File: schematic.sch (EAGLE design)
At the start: 54 parts, among them J1 FTDI_DEVICERA_SMT, M1 WIRELESS-NRF24L01, Q1 8MHz, T1 NMOS, T2 NMOS, T3 NMOS, T4 NMOS, U1 ATMEGA328P_TQFP, U2 GY-521MPU6050, U3 TPS63060

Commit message: Fixed issues mentioned in design review
Changed voltage divider resistors to 10K.
Got new voltage regulator, completely circuit and PCD footprint.
Changed all component package to 0603.
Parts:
- removed C16: 10uF, resistor:C-USC0805K
- removed C17: 0.1uF, resistor:C-USC0201
- added C15: 0.1uF, resistor:C-USC0603
- added R14: 10K, resistor:R-US_R0603
- added R15, R16: 10K, resistor:R-US_M2309
- C12: value 0.1uF -> 27pF; device rcl:C-USC0603 -> resistor:C-USC0603
- C14: value 27pF -> 10uF
- C2: value 10uF -> 0.056uF; device resistor:C-USC0805K -> resistor:C-USC0603
- C3: device resistor:C-USC0805K -> resistor:C-USC0603
- C4: value 0.1uF -> 100pF; device rcl:C-USC0603 -> resistor:C-USC0603
- C5: value 10pF -> 22uF; device rcl:C-USC0603 -> resistor:C-USC0603
- C6: value 22uF -> 470pF; device rcl:C-USC0603 -> resistor:C-USC0603
- C7: value 22uF -> 10pF; device rcl:C-USC0603 -> resistor:C-USC0603
- C8: value 22uF -> 0.1uF
- L1: value 1uH -> 3.3uH
- R11: value 10K -> 820; device resistor:R-US_R0603 -> rcl:R-US_R0603
- R12: value 10K -> 820; device resistor:R-US_M2309 -> rcl:R-US_R0603
- R13: device resistor:R-US_M2309 -> resistor:R-US_R0603
- R2: value 50K -> 10K; device resistor:R-US_M2309 -> resistor:R-US_R0603
- R3: value 150K -> 10K; device resistor:R-US_R0805 -> resistor:R-US_R0603
- R4: value 560K -> 200K; device rcl:R-US_R0805 -> resistor:R-US_R0603
- R5: value 100K -> 10K; device rcl:R-US_R0402 -> resistor:R-US_R0603
- R6: value 820 -> 374K; device rcl:R-US_R0603 -> resistor:R-US_R0603
- R7: value 10K -> 15K
- R8: value 820 -> 162K; device rcl:R-US_R0603 -> resistor:R-US_R0603
- S2: value (none) -> PUSH_BUTTON
- U3: value TPS63060 -> LTC3534; device SparkFun-PowerIC:TPS63060 -> LTC3534:LTC3534
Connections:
- removed net N$27: L1.1, U3.L1
- removed net N$28: L1.2, U3.L2
- removed net N$32: C5.1, R4.1, R5.2, U3.FB
- removed net N$33: C4.1, U3.VAUX
- new net N$15: C4.1, R5.1
- new net N$16: C2.1, R4.1, U3.RUN/SS
- new net N$18: C4.2, C7.2, R6.1, R7.1, R8.2, U3.FB
- new net N$19: C6.1, C7.1, U3.VC
- new net N$20: C6.2, R7.2
- new net N$8: L1.1, U3.SW1
- new net N$9: L1.2, U3.SW2
- net DEBUG_LED1: now also R12.2; no longer R9.2
- net DEBUG_LED2: now also R11.2; no longer R8.2
- net DTR: now also C8.1; no longer C9.1
- net GND: now also C15.2, C9.2, R13.1, R14.1, R15.2, R16.2, R8.1, U3.GND1, U3.GND2, U3.GND3, U3.GND4, U3.GND5, U3.PGND1, U3.PGND2; no longer C16.2, C17.2, C4.2, C6.2, C7.2, C8.2, R10.1, R11.1, R12.2, R13.2, R5.1, U3.GND, U3.PGND@1, U3.PGND@2, U3.PGND@3, U3.PGND@4, U3.PGND@5, U3.PGND@6, U3.PGND@7, U3.PGND@8, U3.PGND@PAD, U3.PS/SYNC
- net N$1: now also C12.1; no longer C13.1
- net N$11: now also R9.1; no longer R6.1
- net N$12: now also R12.1; no longer R9.1
- net N$13: now also R11.1; no longer R8.1
- net N$2: now also C8.2, R10.1; no longer C9.2, R7.1
- net N$25: now also C11.1; no longer C12.1
- net N$4: now also C13.1; no longer C14.1
- net PWM1: now also R13.2; no longer R10.2
- net PWM2: now also R14.2; no longer R11.2
- net PWM3: now also R15.1; no longer R12.1
- net PWM4: now also R16.1; no longer R13.1
- net PWR: now also R4.2, U3.PVIN, U3.PWM; no longer C2.1, U3.EN
- net V_REG_OUT: now also C14.1, C15.1, C5.1, C9.1, R10.2, R5.2, R9.2; no longer C11.1, C16.1, C17.1, C6.1, C7.1, C8.1, R4.2, R7.2
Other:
- moved on the sheet: C1, C10, C11, C12, C13, C14, C2, C3, C4, C5, C6, C7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

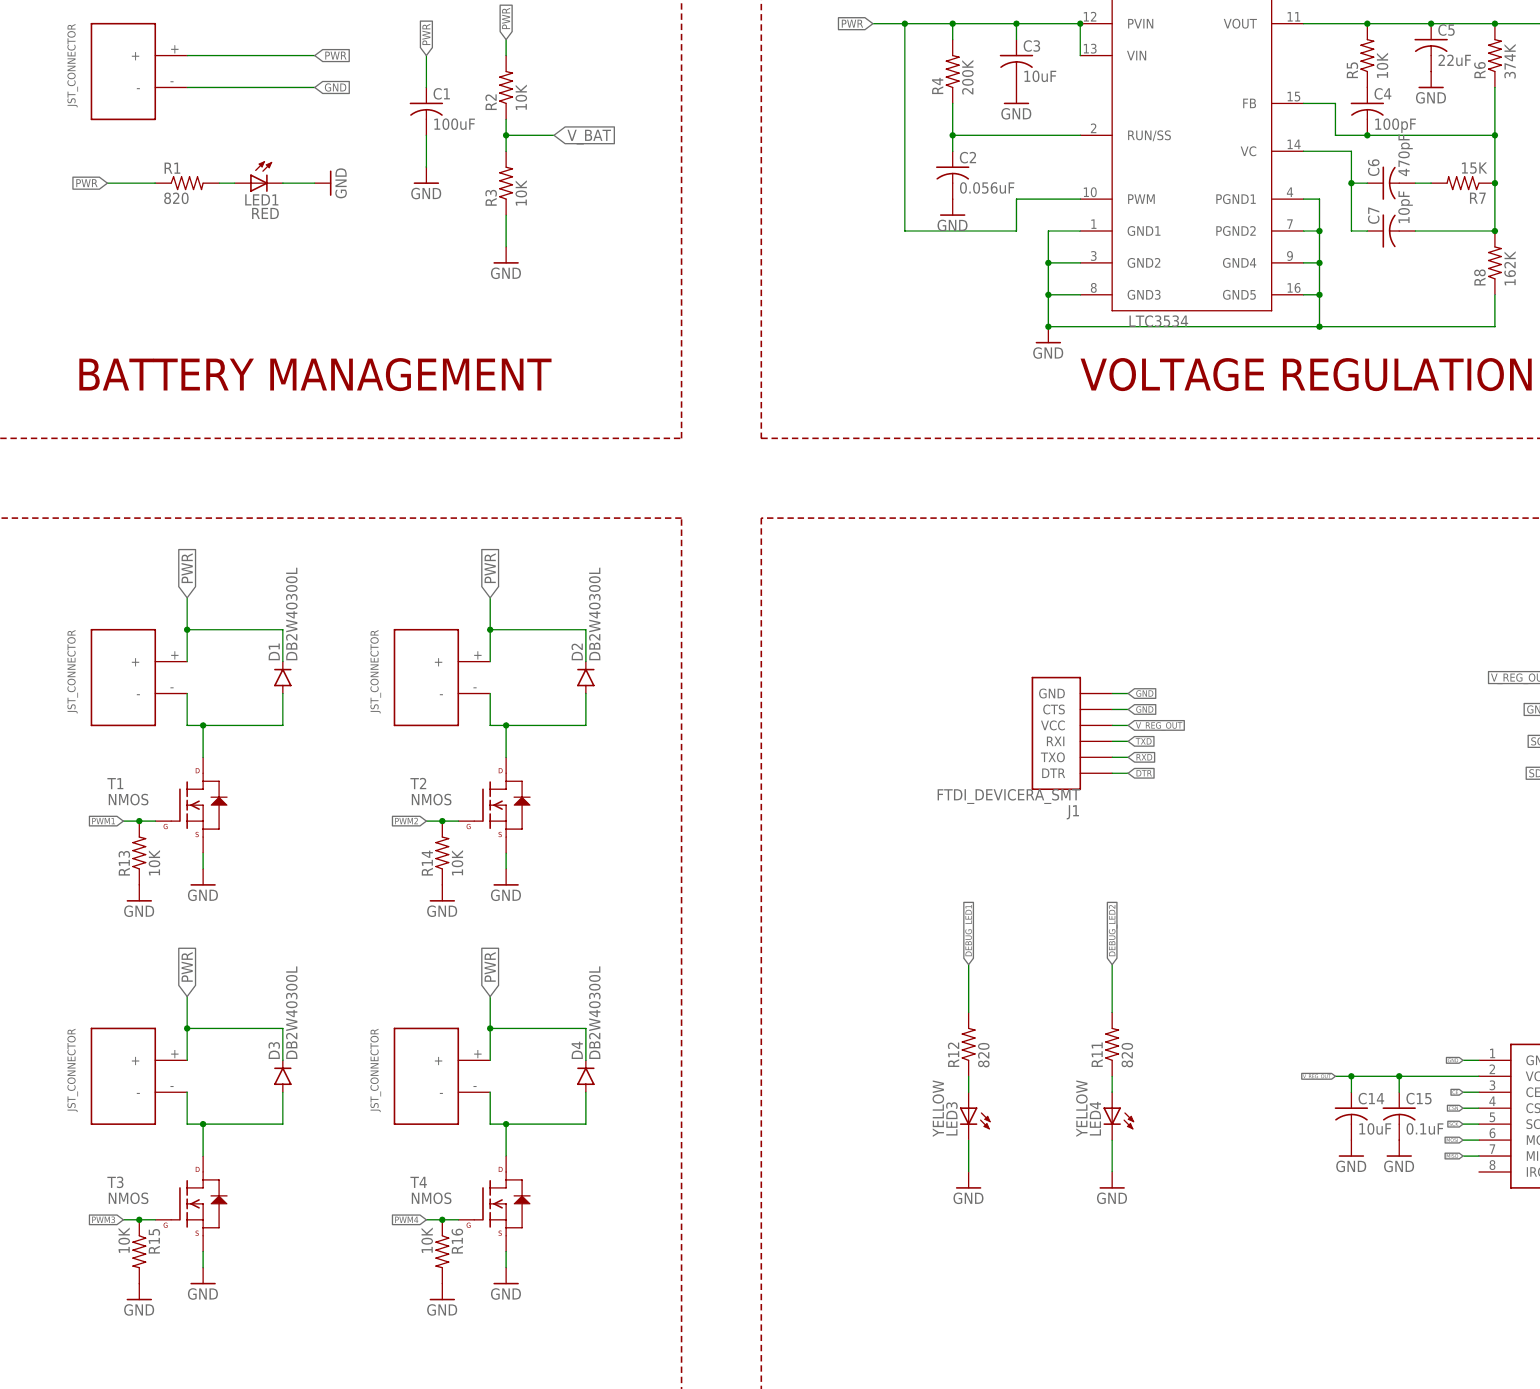
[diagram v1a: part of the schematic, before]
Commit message: Fixed issues from schematic pre-check
Changed package of R15,R16 to 0603.
CHange 100pF capacitor to 68pF to be closer to recommended value.
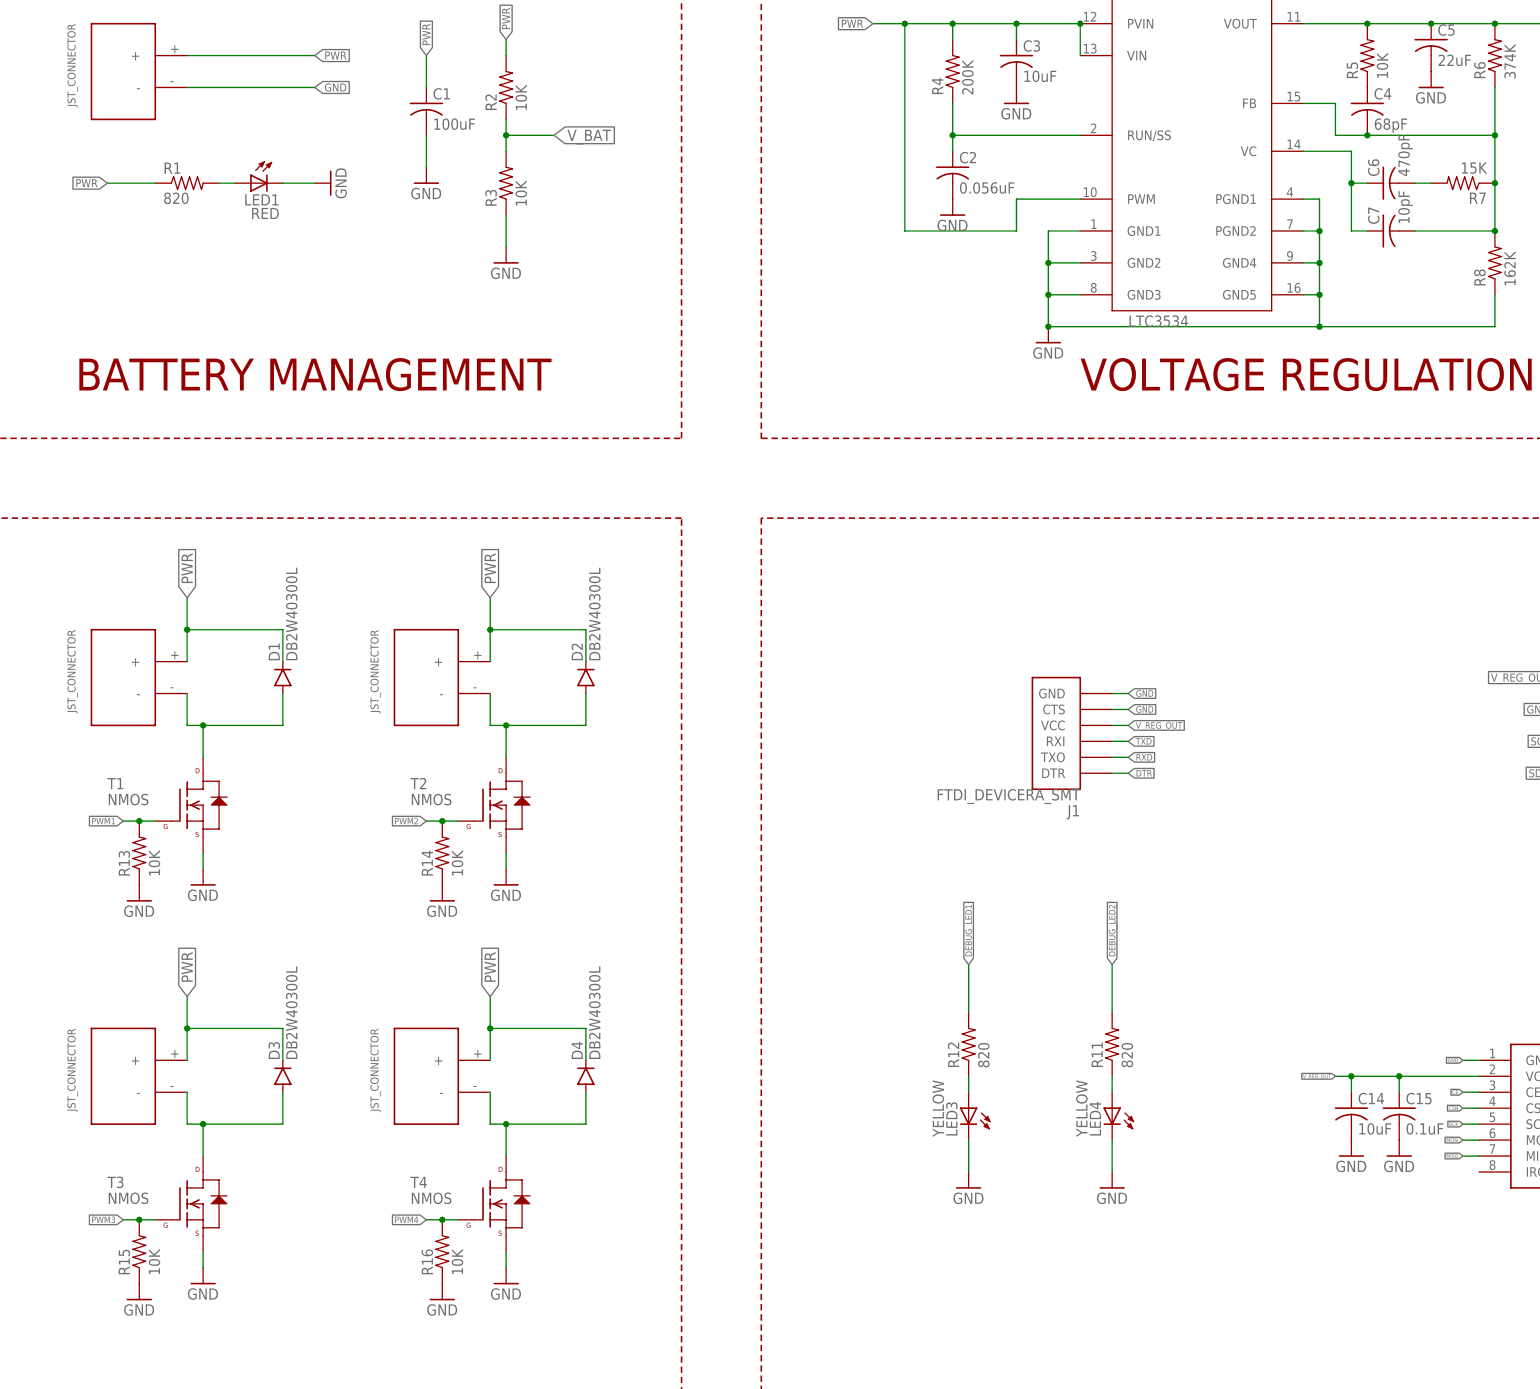
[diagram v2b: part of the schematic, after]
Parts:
- C4: value 100pF -> 68pF
- R15, R16: device resistor:R-US_M2309 -> resistor:R-US_R0603
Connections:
- net GND: now also R15.1, R16.1; no longer R15.2, R16.2
- net PWM3: now also R15.2; no longer R15.1
- net PWM4: now also R16.2; no longer R16.1
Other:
- moved on the sheet: R15, R16
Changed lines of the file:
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@@
 <part name="R13" library="resistor" library_urn="urn:adsk.eagle:library:348" deviceset="R-US_" device="R0603" package3d_urn="urn:adsk.eagle:package:26057/1" value="10K"/>
 <part name="R14" library="resistor" library_urn="urn:adsk.eagle:library:348" deviceset="R-US_" device="R0603" package3d_urn="urn:adsk.eagle:package:26057/1" value="10K"/>
-<part name="R15" library="resistor" library_urn="urn:adsk.eagle:library:348" deviceset="R-US_" device="M2309" package3d_urn="urn:adsk.eagle:package:26085/1" value="10K"/>
-<part name="R16" library="resistor" library_urn="urn:adsk.eagle:library:348" deviceset="R-US_" device="M2309" package3d_urn="urn:adsk.eagle:package:26085/1" value="10K"/>
 <part name="C1" library="rcl" library_urn="urn:adsk.eagle:library:334" deviceset="C-US" device="C1210" package3d_urn="urn:adsk.eagle:package:23619/2" value="100uF"/>
 <part name="C8" library="rcl" library_urn="urn:adsk.eagle:library:334" deviceset="C-US" device="C0603" package3d_urn="urn:adsk.eagle:package:23616/2" value="0.1uF"/>
@@
 <part name="C3" library="resistor" library_urn="urn:adsk.eagle:library:348" deviceset="C-US" device="C0603" package3d_urn="urn:adsk.eagle:package:26138/1" value="10uF"/>
 <part name="R5" library="resistor" library_urn="urn:adsk.eagle:library:348" deviceset="R-US_" device="R0603" package3d_urn="urn:adsk.eagle:package:26057/1" value="10K"/>
-<part name="C4" library="resistor" library_urn="urn:adsk.eagle:library:348" deviceset="C-US" device="C0603" package3d_urn="urn:adsk.eagle:package:26138/1" value="100pF"/>
+<part name="C4" library="resistor" library_urn="urn:adsk.eagle:library:348" deviceset="C-US" device="C0603" package3d_urn="urn:adsk.eagle:package:26138/1" value="68pF"/>
 <part name="C5" library="resistor" library_urn="urn:adsk.eagle:library:348" deviceset="C-US" device="C0603" package3d_urn="urn:adsk.eagle:package:26138/1" value="22uF"/>
 <part name="R6" library="resistor" library_urn="urn:adsk.eagle:library:348" deviceset="R-US_" device="R0603" package3d_urn="urn:adsk.eagle:package:26057/1" value="374K"/>
@@
 <part name="C14" library="resistor" library_urn="urn:adsk.eagle:library:348" deviceset="C-US" device="C0603" package3d_urn="urn:adsk.eagle:package:26138/1" value="10uF"/>
 <part name="C15" library="resistor" library_urn="urn:adsk.eagle:library:348" deviceset="C-US" device="C0603" package3d_urn="urn:adsk.eagle:package:26138/1" value="0.1uF"/>
+<part name="R15" library="resistor" library_urn="urn:adsk.eagle:library:348" deviceset="R-US_" device="R0603" package3d_urn="urn:adsk.eagle:package:26057/1" value="10K"/>
+<part name="R16" library="resistor" library_urn="urn:adsk.eagle:library:348" deviceset="R-US_" device="R0603" package3d_urn="urn:adsk.eagle:package:26057/1" value="10K"/>
 </parts>
 <sheets>
@@
 <instance part="R13" gate="G$1" x="-193.04" y="-2.54" rot="R90"/>
 <instance part="R14" gate="G$1" x="-144.78" y="-2.54" rot="R90"/>
-<instance part="R15" gate="G$1" x="-193.04" y="-66.04" rot="R270"/>
-<instance part="R16" gate="G$1" x="-144.78" y="-66.04" rot="R270"/>
 <instance part="C1" gate="G$1" x="-147.32" y="116.84"/>
 <instance part="C8" gate="G$1" x="132.08" y="106.68" rot="R90"/>
@@
 <instance part="C14" gate="G$1" x="0" y="-43.18"/>
 <instance part="C15" gate="G$1" x="7.62" y="-43.18"/>
+<instance part="R15" gate="G$1" x="-193.04" y="-66.04" rot="R90"/>
+<instance part="R16" gate="G$1" x="-144.78" y="-66.04" rot="R90"/>
 </instances>
 <busses>
@@
 <pinref part="GND27" gate="1" pin="GND"/>
 <pinref part="R14" gate="G$1" pin="1"/>
-</segment>
-<segment>
-<pinref part="GND28" gate="1" pin="GND"/>
-<pinref part="R15" gate="G$1" pin="2"/>
-</segment>
-<segment>
-<pinref part="GND29" gate="1" pin="GND"/>
-<pinref part="R16" gate="G$1" pin="2"/>
 </segment>
 <segment>
@@
 <pinref part="C15" gate="G$1" pin="2"/>
 </segment>
+<segment>
+<pinref part="GND28" gate="1" pin="GND"/>
+<pinref part="R15" gate="G$1" pin="1"/>
+</segment>
+<segment>
+<pinref part="GND29" gate="1" pin="GND"/>
+<pinref part="R16" gate="G$1" pin="1"/>
+</segment>
 </net>
 <net name="N$4" class="0">
@@
 <segment>
 <pinref part="T3" gate="G$1" pin="G"/>
+<label x="-195.58" y="-60.96" size="1.016" layer="95" rot="R180" xref="yes"/>
 <wire x1="-190.5" y1="-60.96" x2="-193.04" y2="-60.96" width="0.1524" layer="91"/>
-<label x="-195.58" y="-60.96" size="1.016" layer="95" rot="R180" xref="yes"/>
-<pinref part="R15" gate="G$1" pin="1"/>
+<pinref part="R15" gate="G$1" pin="2"/>
 <wire x1="-193.04" y1="-60.96" x2="-195.58" y2="-60.96" width="0.1524" layer="91"/>
 <junction x="-193.04" y="-60.96"/>
@@
 <segment>
 <pinref part="T4" gate="G$1" pin="G"/>
+<label x="-147.32" y="-60.96" size="1.016" layer="95" rot="R180" xref="yes"/>
 <wire x1="-142.24" y1="-60.96" x2="-144.78" y2="-60.96" width="0.1524" layer="91"/>
-<label x="-147.32" y="-60.96" size="1.016" layer="95" rot="R180" xref="yes"/>
-<pinref part="R16" gate="G$1" pin="1"/>
+<pinref part="R16" gate="G$1" pin="2"/>
 <wire x1="-144.78" y1="-60.96" x2="-147.32" y2="-60.96" width="0.1524" layer="91"/>
 <junction x="-144.78" y="-60.96"/>

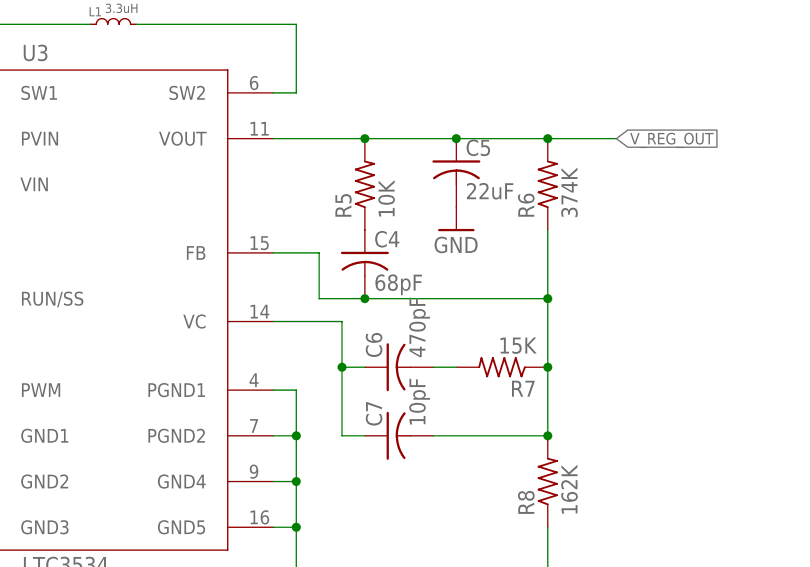
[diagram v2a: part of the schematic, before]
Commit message: 65pF capacitor 1206 package
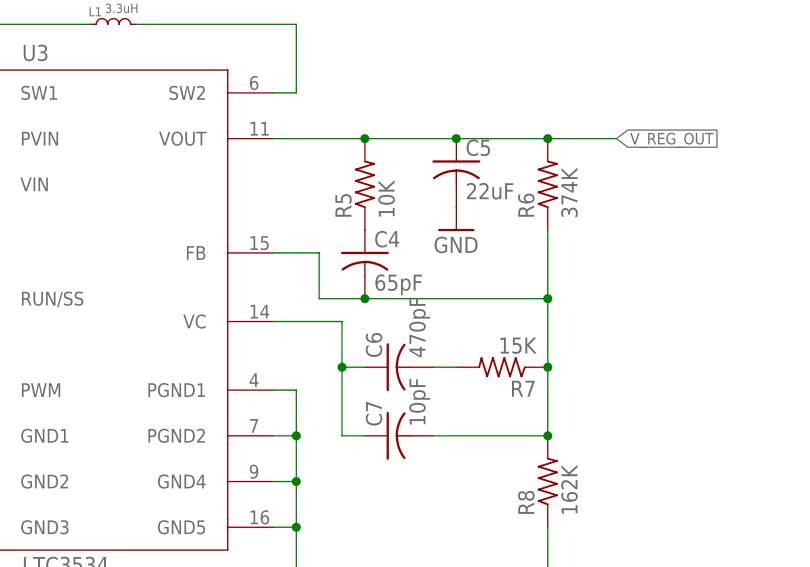
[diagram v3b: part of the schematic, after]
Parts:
- C4: value 68pF -> 65pF; device resistor:C-USC0603 -> rcl:C-USC1206
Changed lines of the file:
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@@
 <part name="C3" library="resistor" library_urn="urn:adsk.eagle:library:348" deviceset="C-US" device="C0603" package3d_urn="urn:adsk.eagle:package:26138/1" value="10uF"/>
 <part name="R5" library="resistor" library_urn="urn:adsk.eagle:library:348" deviceset="R-US_" device="R0603" package3d_urn="urn:adsk.eagle:package:26057/1" value="10K"/>
-<part name="C4" library="resistor" library_urn="urn:adsk.eagle:library:348" deviceset="C-US" device="C0603" package3d_urn="urn:adsk.eagle:package:26138/1" value="68pF"/>
 <part name="C5" library="resistor" library_urn="urn:adsk.eagle:library:348" deviceset="C-US" device="C0603" package3d_urn="urn:adsk.eagle:package:26138/1" value="22uF"/>
 <part name="R6" library="resistor" library_urn="urn:adsk.eagle:library:348" deviceset="R-US_" device="R0603" package3d_urn="urn:adsk.eagle:package:26057/1" value="374K"/>
@@
 <part name="R15" library="resistor" library_urn="urn:adsk.eagle:library:348" deviceset="R-US_" device="R0603" package3d_urn="urn:adsk.eagle:package:26057/1" value="10K"/>
 <part name="R16" library="resistor" library_urn="urn:adsk.eagle:library:348" deviceset="R-US_" device="R0603" package3d_urn="urn:adsk.eagle:package:26057/1" value="10K"/>
+<part name="C4" library="rcl" library_urn="urn:adsk.eagle:library:334" deviceset="C-US" device="C1206" package3d_urn="urn:adsk.eagle:package:23618/2" value="65pF"/>
 </parts>
 <sheets>
@@
 <instance part="C3" gate="G$1" x="-53.34" y="124.46"/>
 <instance part="R5" gate="G$1" x="2.54" y="124.46" rot="R90"/>
-<instance part="C4" gate="G$1" x="2.54" y="116.84"/>
 <instance part="C5" gate="G$1" x="12.7" y="127"/>
 <instance part="R6" gate="G$1" x="22.86" y="124.46" rot="R90"/>
@@
 <instance part="R15" gate="G$1" x="-193.04" y="-66.04" rot="R90"/>
 <instance part="R16" gate="G$1" x="-144.78" y="-66.04" rot="R90"/>
+<instance part="C4" gate="G$1" x="2.54" y="116.84"/>
 </instances>
 <busses>
@@
 <wire x1="22.86" y1="96.52" x2="10.16" y2="96.52" width="0.1524" layer="91"/>
 <wire x1="22.86" y1="111.76" x2="22.86" y2="104.14" width="0.1524" layer="91"/>
-<pinref part="C4" gate="G$1" pin="2"/>
-<junction x="2.54" y="111.76"/>
 <pinref part="R6" gate="G$1" pin="1"/>
 <pinref part="R8" gate="G$1" pin="2"/>
@@
 <junction x="22.86" y="104.14"/>
 <pinref part="C7" gate="G$1" pin="2"/>
+<pinref part="C4" gate="G$1" pin="2"/>
+<junction x="2.54" y="111.76"/>
 </segment>
 </net>
@@
 </segment>
 </net>
-<net name="N$15" class="0">
+<net name="N$14" class="0">
 <segment>
 <pinref part="R5" gate="G$1" pin="1"/>
